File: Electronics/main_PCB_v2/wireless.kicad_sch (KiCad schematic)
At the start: 36 parts, among them J401 Conn_Coaxial, U401 NRF24L01, U402 RFX2401C, Y402 16M

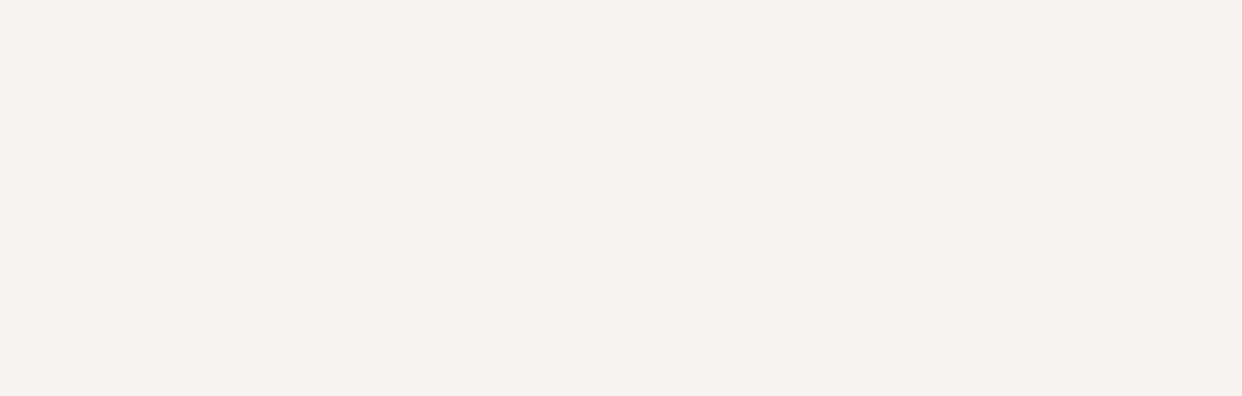
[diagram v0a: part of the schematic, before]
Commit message: Updated PCB outlines
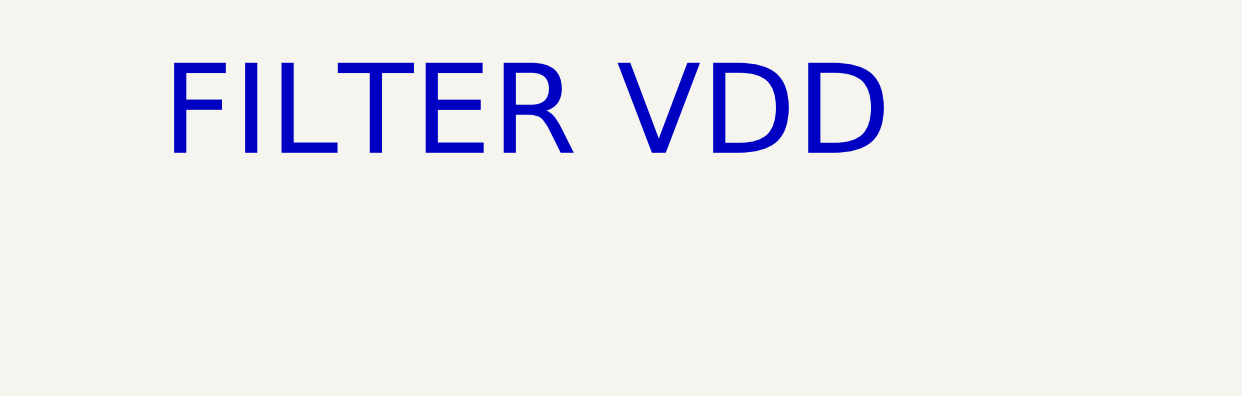
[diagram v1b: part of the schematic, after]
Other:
- note added: "FILTER VDD"
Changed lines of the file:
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@@
     (stroke (width 0) (type default))
+  )
+  (text "FILTER VDD" (at 91.44 68.58 0)
+    (effects (font (size 10 10)) (justify left bottom))
   )
   (text "Potential divider\nbecause VCTL max\nvoltage is 1.8V"
